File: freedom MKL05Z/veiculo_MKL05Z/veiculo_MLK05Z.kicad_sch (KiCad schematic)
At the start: 58 parts, among them J1 Conn_01x02_Male, J10 Conn_01x02_Male, J11 Conn_01x02_Male, J12 Conn_01x02_Male, J13 Conn_01x02_Male, J14 Conn_01x02_Male, J15 Conn_01x02_Male, J16 Conn_01x02_Male, J17 Conn_01x02_Male, J18 Conn_01x02_Male, J19 Conn_01x02_Male, J2 Conn_01x02_Male, J20 Conn_01x02_Male, J21 Conn_01x02_Male, J23 Conn_01x04_Male, J3 Conn_01x02_Male, J4 Conn_01x02_Male, J5 Conn_01x02_Male, J6 Conn_01x02_Male, J7 Conn_02x13_Odd_Even, J8 Conn_01x02_Male, J9 Conn_01x02_Male, P1 Power, P2 Analog, P3 Digital, P4 Digital, P6 CONN_01X01, P7 CONN_01X01, P8 CONN_01X01, Q1 2N7002, Q3 2N7002, Q4 2N7002, Q5 2N7002, Q6 2N7002, Q7 2N7002, Q8 2N7002, Q9 2N7002

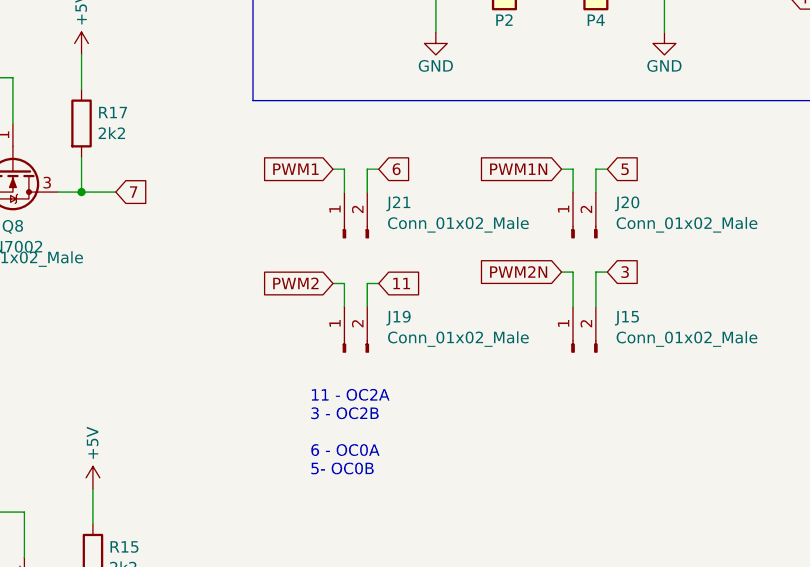
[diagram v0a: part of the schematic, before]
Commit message: Created README.md to MKL05Z Shield
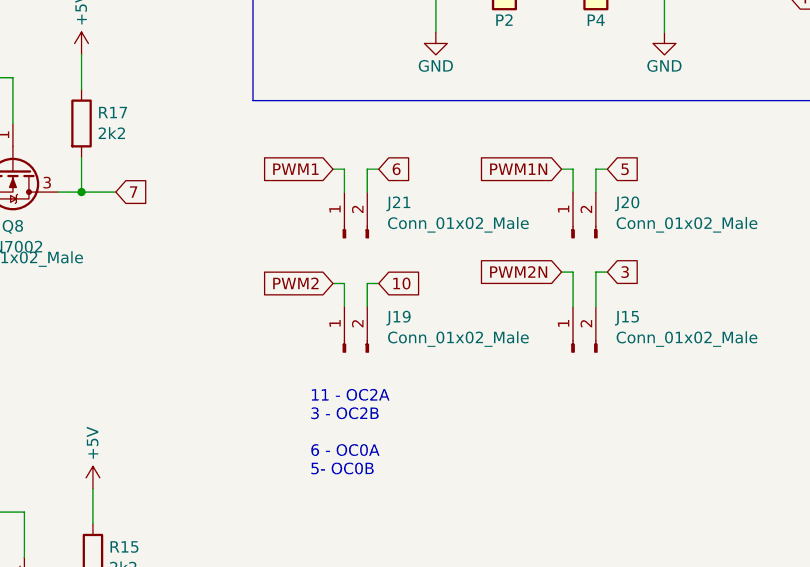
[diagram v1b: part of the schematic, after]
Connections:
- net 10: now also J19.2 (Pin_2)
- net 11: no longer J19.2 (Pin_2)
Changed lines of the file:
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@@
     )
   )
-  (global_label "11" (shape input) (at 229.87 107.95 0) (fields_autoplaced)
+  (global_label "10" (shape input) (at 229.87 107.95 0) (fields_autoplaced)
     (effects (font (size 1.27 1.27)) (justify left))
     (property "Intersheetrefs" "${INTERSHEET_REFS}" (at 234.62 107.95 0)
